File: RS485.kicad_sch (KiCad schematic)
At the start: 0 parts

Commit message: Latest updates
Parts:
- added C17: 0.1u, symbol Device:C
- added J11: Screw_Terminal_01x05, symbol Connector:Screw_Terminal_01x05
- added R14: 120, symbol Device:R
- added SW3: SW_DIP_x03, symbol Switch:SW_DIP_x03
- added U3: SIT3490EESA, EasyEDA:SOP-8_L4.9-W3.9-P1.27-LS6.0-BL, symbol EasyEDA:SIT3490EESA
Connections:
- new net: R14.1, SW3.6
- new net +3.3V: C17.1, U3.1 (VCC)
- new net A: J11.3 (Pin_3), SW3.1, SW3.2, U3.8 (A)
- new net B: J11.4 (Pin_4), R14.2, SW3.3, U3.7 (B)
- new net DI: U3.3 (DI)
- new net GND: C17.2, J11.5 (Pin_5), U3.4 (GND)
- new net RO: U3.2 (RO)
- new net Y: J11.1 (Pin_1), SW3.4, U3.5 (Y)
- new net Z: J11.2 (Pin_2), SW3.5, U3.6 (Z)
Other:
- note added: "RS485 Full-Duplex Tranciver"
- note added: "The dip switch array adds optional Termination and Half-Duplex mode 1-6 closed (Termination enabled between A-B) 2-5 closed and 3-4 closed (A-Z and B-Y shorted) for half duplex mode (Software realization should be added for self talk ignorance)"

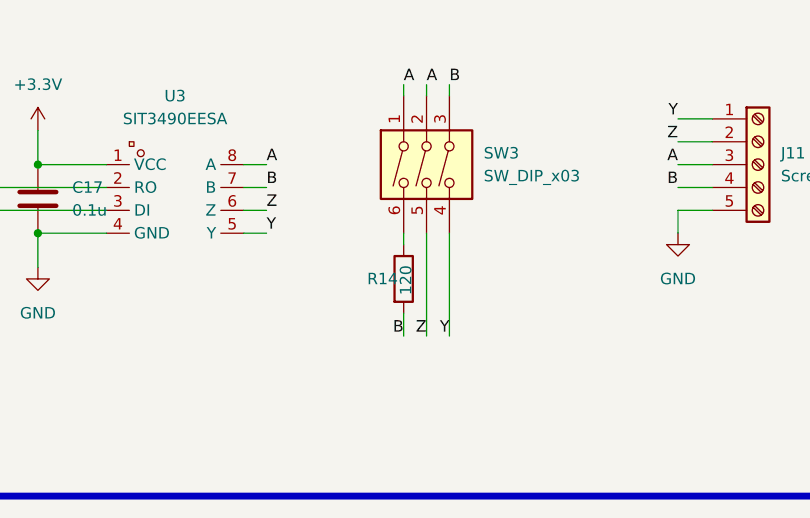
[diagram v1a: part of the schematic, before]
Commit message: Schematic--Footprint link
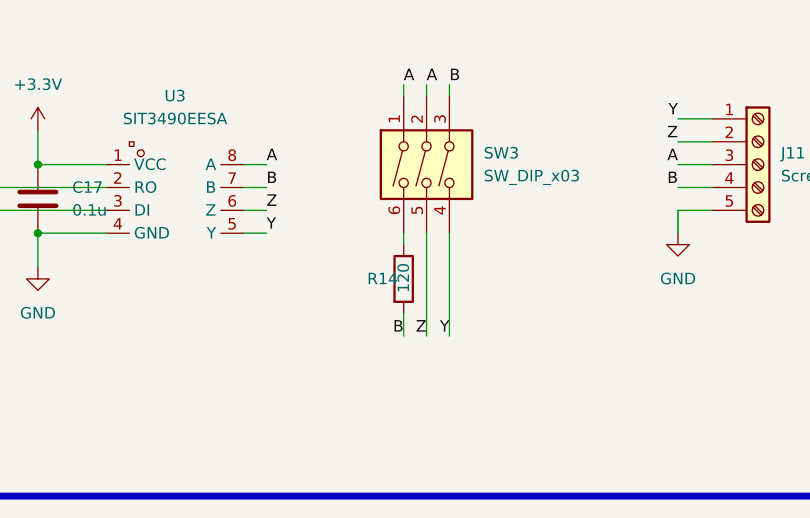
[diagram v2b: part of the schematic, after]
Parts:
- C17: footprint (none) -> Capacitor_SMD:C_0805_2012Metric
- J11: footprint (none) -> TerminalBlock_Phoenix:TerminalBlock_Phoenix_PT-1,5-5-3.5-H_1x05_P3.50mm_Horizontal
- R14: footprint (none) -> Resistor_SMD:R_0805_2012Metric
- SW3: footprint (none) -> Button_Switch_THT:SW_DIP_SPSTx03_Slide_6.7x9.18mm_W7.62mm_P2.54mm_LowProfile
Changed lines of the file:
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@@
 			)
 		)
-		(property "Footprint" ""
+		(property "Footprint" "Button_Switch_THT:SW_DIP_SPSTx03_Slide_6.7x9.18mm_W7.62mm_P2.54mm_LowProfile"
 			(at 142.24 96.52 0)
 			(effects
@@
 			)
 		)
-		(property "Footprint" ""
+		(property "Footprint" "TerminalBlock_Phoenix:TerminalBlock_Phoenix_PT-1,5-5-3.5-H_1x05_P3.50mm_Horizontal"
 			(at 176.53 96.52 0)
 			(effects
@@
 			)
 		)
-		(property "Footprint" ""
+		(property "Footprint" "Capacitor_SMD:C_0805_2012Metric"
 			(at 97.4852 104.14 0)
 			(effects
@@
 		)
 		(property "Value" "120"
-			(at 137.414 107.696 90)
+			(at 137.16 107.442 90)
 			(effects
 				(font
@@
 			)
 		)
-		(property "Footprint" ""
+		(property "Footprint" "Resistor_SMD:R_0805_2012Metric"
 			(at 135.382 109.22 90)
 			(effects
